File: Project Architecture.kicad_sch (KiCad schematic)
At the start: 0 parts

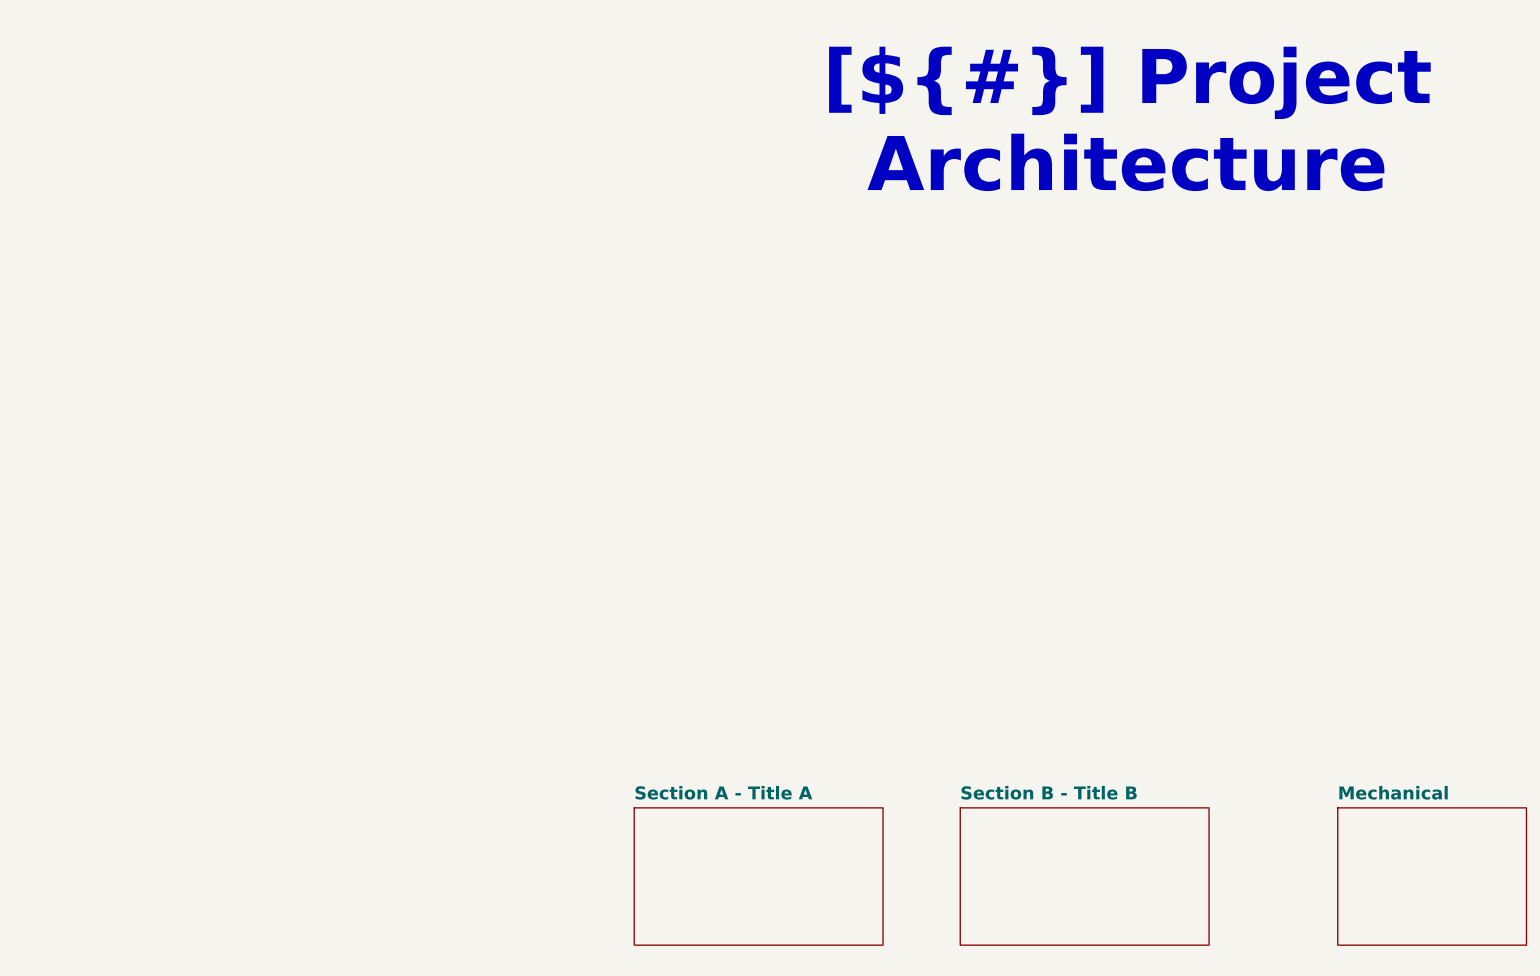
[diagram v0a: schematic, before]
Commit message: SCH[Inital Setup]: Created intital pages, added some inital symbols.
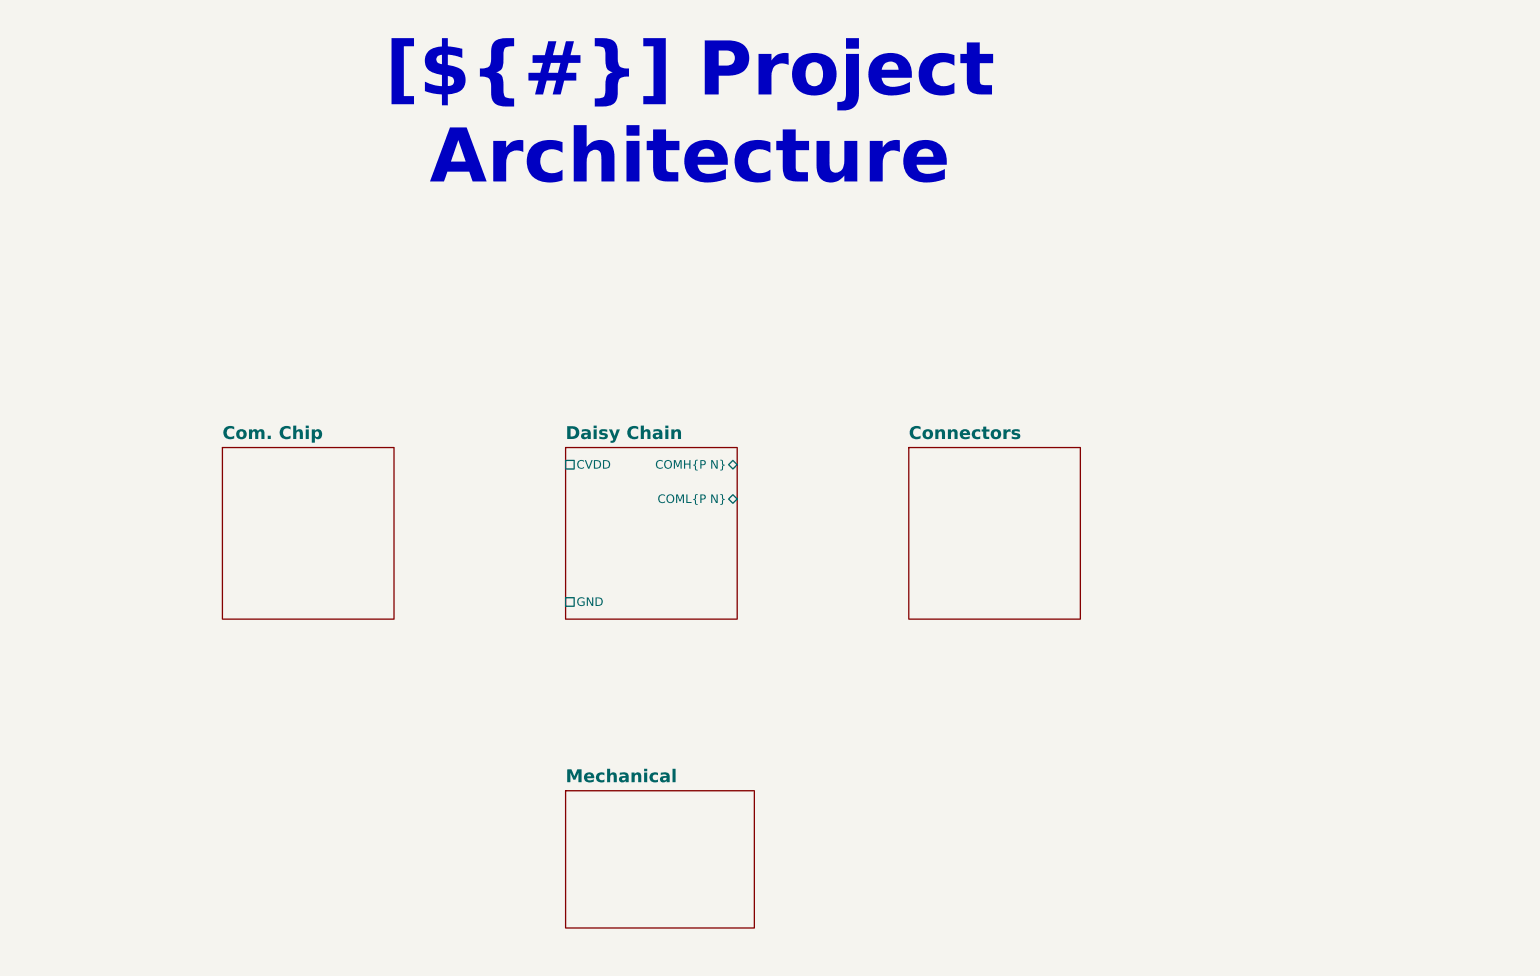
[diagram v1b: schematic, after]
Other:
- removed sheet Section A - Title A
- removed sheet Section B - Title B
- added sheet Com. Chip (com_chip.kicad_sch)
- added sheet Connectors (connectors.kicad_sch)
- added sheet Daisy Chain (daisy_chain.kicad_sch)
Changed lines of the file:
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@@
 	(generator "eeschema")
 	(generator_version "10.0")
-	(paper "A3")
+	(paper "A4")
 	(title_block
 		(title "Project Architecture")
@@
 	(text_box "[${#}] ${TITLE}"
 		(exclude_from_sim no)
-		(at 144.78 21.59 0)
+		(at 80.01 20.32 0)
 		(size 130.81 12.7)
 		(margins 5.9999 5.9999 5.9999 5.9999)
@@
 	)
 	(sheet
-		(at 241.3 129.54)
+		(at 177.8 76.2)
+		(size 25.4 25.4)
+		(exclude_from_sim no)
+		(in_bom yes)
+		(on_board yes)
+		(dnp no)
+		(fields_autoplaced yes)
+		(stroke
+			(width 0.1524)
+			(type solid)
+		)
+		(fill
+			(color 255 255 194 1)
+		)
+		(property "Sheetname" "Connectors"
+			(at 177.8 75.1709 0)
+			(show_name no)
+			(do_not_autoplace no)
+			(effects
+				(font
+					(size 1.905 1.905)
+					(thickness 0.254)
+					(bold yes)
+				)
+				(justify left bottom)
+			)
+		)
+		(property "Sheetfile" "connectors.kicad_sch"
+			(at 177.8 102.1846 0)
+			(hide yes)
+			(show_name no)
+			(do_not_autoplace no)
+			(effects
+				(font
+					(size 1.27 1.27)
+				)
+				(justify left top)
+			)
+		)
+		(instances
+			(project "bms_master"
+				(path "/f9e05184-c88b-4a88-ae9c-ab2bdb32be7c/c5103ceb-5325-4a84-a025-9638a412984e"
+					(page "4")
+				)
+			)
+		)
+	)
+	(sheet
+		(at 127 76.2)
+		(size 25.4 25.4)
+		(exclude_from_sim no)
+		(in_bom yes)
+		(on_board yes)
+		(dnp no)
+		(fields_autoplaced yes)
+		(stroke
+			(width 0)
+			(type solid)
+		)
+		(fill
+			(color 255 255 194 1)
+		)
+		(property "Sheetname" "Daisy Chain"
+			(at 127 75.1709 0)
+			(show_name no)
+			(do_not_autoplace no)
+			(effects
+				(font
+					(size 1.905 1.905)
+					(thickness 0.254)
+					(bold yes)
+				)
+				(justify left bottom)
+			)
+		)
+		(property "Sheetfile" "daisy_chain.kicad_sch"
+			(at 127 102.1846 0)
+			(hide yes)
+			(show_name no)
+			(do_not_autoplace no)
+			(effects
+				(font
+					(size 1.27 1.27)
+				)
+				(justify left top)
+			)
+		)
+		(pin "CVDD" passive
+			(at 127 78.74 180)
+			(effects
+				(font
+					(size 1.27 1.27)
+				)
+				(justify left)
+			)
+		)
+		(pin "GND" passive
+			(at 127 99.06 180)
+			(effects
+				(font
+					(size 1.27 1.27)
+				)
+				(justify left)
+			)
+		)
+		(pin "COMH{P N}" bidirectional
+			(at 152.4 78.74 0)
+			(effects
+				(font
+					(size 1.27 1.27)
+				)
+				(justify right)
+			)
+		)
+		(pin "COML{P N}" bidirectional
+			(at 152.4 83.82 0)
+			(effects
+				(font
+					(size 1.27 1.27)
+				)
+				(justify right)
+			)
+		)
+		(instances
+			(project "bms_master"
+				(path "/f9e05184-c88b-4a88-ae9c-ab2bdb32be7c/c5103ceb-5325-4a84-a025-9638a412984e"
+					(page "6")
+				)
+			)
+		)
+	)
+	(sheet
+		(at 127 127)
 		(size 27.94 20.32)
 		(exclude_from_sim no)
@@
 		)
 		(property "Sheetname" "Mechanical"
-			(at 241.3 128.5109 0)
+			(at 127 125.9709 0)
 			(show_name no)
 			(do_not_autoplace no)
@@
 		)
 		(property "Sheetfile" "mechanical.kicad_sch"
-			(at 241.3 150.4446 0)
-			(hide yes)
-			(show_name no)
-			(do_not_autoplace no)
-			(effects
-				(font
-					(size 1.27 1.27)
-				)
-				(justify left top)
-			)
-		)
-		(instances
-			(project "BOARD_TEMPLATE"
-				(path "/f9e05184-c88b-4a88-ae9c-ab2bdb32be7c/c5103ceb-5325-4a84-a025-9638a412984e"
-					(page "6")
-				)
-			)
-		)
-	)
-	(sheet
-		(at 185.42 129.54)
-		(size 36.83 20.32)
-		(exclude_from_sim no)
-		(in_bom yes)
-		(on_board yes)
-		(dnp no)
-		(fields_autoplaced yes)
-		(stroke
-			(width 0)
-			(type solid)
-		)
-		(fill
-			(color 255 255 194 1)
-		)
-		(property "Sheetname" "Section B - Title B"
-			(at 185.42 128.5109 0)
-			(show_name no)
-			(do_not_autoplace no)
-			(effects
-				(font
-					(size 1.905 1.905)
-					(bold yes)
-				)
-				(justify left bottom)
-			)
-		)
-		(property "Sheetfile" "Section B - Title B.kicad_sch"
-			(at 185.42 150.4446 0)
-			(hide yes)
-			(show_name no)
-			(do_not_autoplace no)
-			(effects
-				(font
-					(face "Arial")
-					(size 1.27 1.27)
-				)
-				(justify left top)
-			)
-		)
-		(instances
-			(project "BOARD_TEMPLATE"
+			(at 127 147.9046 0)
+			(hide yes)
+			(show_name no)
+			(do_not_autoplace no)
+			(effects
+				(font
+					(size 1.27 1.27)
+				)
+				(justify left top)
+			)
+		)
+		(instances
+			(project "bms_master"
+				(path "/f9e05184-c88b-4a88-ae9c-ab2bdb32be7c/c5103ceb-5325-4a84-a025-9638a412984e"
+					(page "8")
+				)
+			)
+		)
+	)
+	(sheet
+		(at 76.2 76.2)
+		(size 25.4 25.4)
+		(exclude_from_sim no)
+		(in_bom yes)
+		(on_board yes)
+		(dnp no)
+		(fields_autoplaced yes)
+		(stroke
+			(width 0.1524)
+			(type solid)
+		)
+		(fill
+			(color 255 255 194 1)
+		)
+		(property "Sheetname" "Com. Chip"
+			(at 76.2 75.1709 0)
+			(show_name no)
+			(do_not_autoplace no)
+			(effects
+				(font
+					(size 1.905 1.905)
+					(thickness 0.254)
+					(bold yes)
+				)
+				(justify left bottom)
+			)
+		)
+		(property "Sheetfile" "com_chip.kicad_sch"
+			(at 76.2 102.1846 0)
+			(hide yes)
+			(show_name no)
+			(do_not_autoplace no)
+			(effects
+				(font
+					(size 1.27 1.27)
+				)
+				(justify left top)
+			)
+		)
+		(instances
+			(project "bms_master"
 				(path "/f9e05184-c88b-4a88-ae9c-ab2bdb32be7c/c5103ceb-5325-4a84-a025-9638a412984e"
 					(page "5")
 				)
 			)
-		)
-	)
-	(sheet
-		(at 137.16 129.54)
-		(size 36.83 20.32)
-		(exclude_from_sim no)
-		(in_bom yes)
-		(on_board yes)
-		(dnp no)
-		(fields_autoplaced yes)
-		(stroke
-			(width 0)
-			(type solid)
-		)
-		(fill
-			(color 255 255 194 1)
-		)
-		(property "Sheetname" "Section A - Title A"
-			(at 137.16 128.5109 0)
-			(show_name no)
-			(do_not_autoplace no)
-			(effects
-				(font
-					(size 1.905 1.905)
-					(bold yes)
-				)
-				(justify left bottom)
-			)
-		)
-		(property "Sheetfile" "Section A - Title A.kicad_sch"
-			(at 137.16 150.4446 0)
-			(hide yes)
-			(show_name no)
-			(do_not_autoplace no)
-			(effects
-				(font
-					(face "Arial")
-					(size 1.27 1.27)
-				)
-				(justify left top)
-			)
-		)
-		(instances
-			(project "BOARD_TEMPLATE"
-				(path "/f9e05184-c88b-4a88-ae9c-ab2bdb32be7c/c5103ceb-5325-4a84-a025-9638a412984e"
-					(page "4")
-				)
-			)

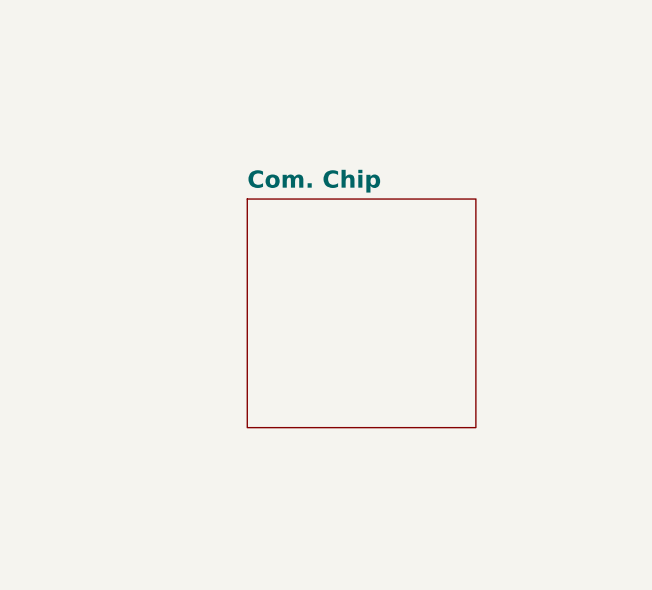
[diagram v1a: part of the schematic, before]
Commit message: SCH[Connecotr]: Added tim pinout.
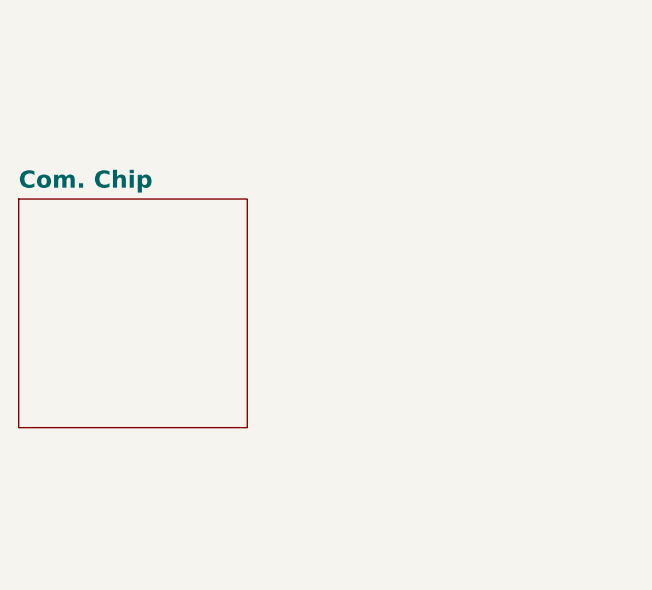
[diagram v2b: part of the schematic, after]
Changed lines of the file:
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@@
 	)
 	(sheet
-		(at 76.2 76.2)
+		(at 50.8 76.2)
 		(size 25.4 25.4)
 		(exclude_from_sim no)
@@
 		)
 		(property "Sheetname" "Com. Chip"
-			(at 76.2 75.1709 0)
+			(at 50.8 75.1709 0)
 			(show_name no)
 			(do_not_autoplace no)
@@
 		)
 		(property "Sheetfile" "com_chip.kicad_sch"
-			(at 76.2 102.1846 0)
+			(at 50.8 102.1846 0)
 			(hide yes)
 			(show_name no)

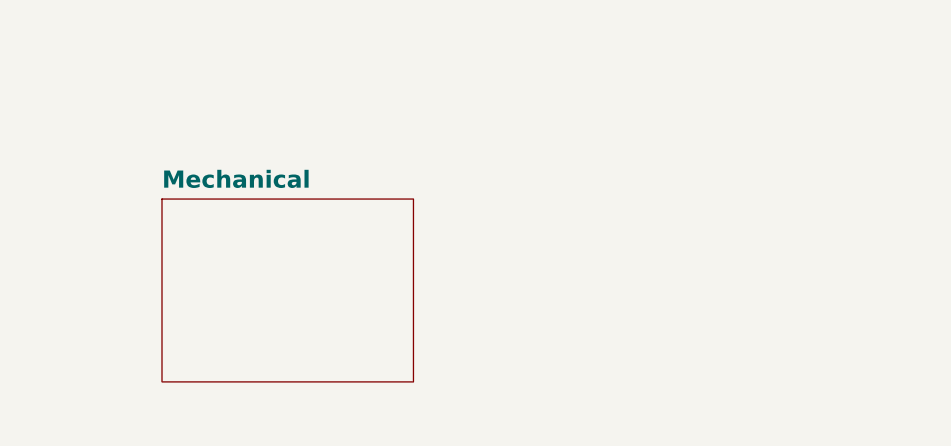
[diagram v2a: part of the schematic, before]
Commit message: SCH[Pages, Chips]: Created page setup, and placed main IC's.
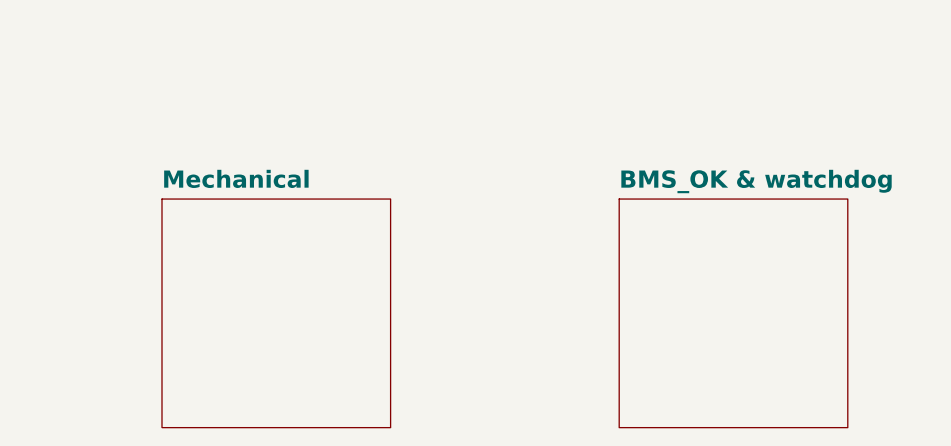
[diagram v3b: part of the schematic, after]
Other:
- added sheet BMS_OK & watchdog (bms_ok_and_watchdog.kicad_sch)
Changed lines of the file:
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@@
+	)
+	(sheet
+		(at 177.8 127)
+		(size 25.4 25.4)
+		(exclude_from_sim no)
+		(in_bom yes)
+		(on_board yes)
+		(dnp no)
+		(fields_autoplaced yes)
+		(stroke
+			(width 0)
+			(type solid)
+		)
+		(fill
+			(color 255 255 194 1)
+		)
+		(property "Sheetname" "BMS_OK & watchdog"
+			(at 177.8 125.9709 0)
+			(show_name no)
+			(do_not_autoplace no)
+			(effects
+				(font
+					(size 1.905 1.905)
+					(thickness 0.381)
+					(bold yes)
+				)
+				(justify left bottom)
+			)
+		)
+		(property "Sheetfile" "bms_ok_and_watchdog.kicad_sch"
+			(at 177.8 152.9846 0)
+			(hide yes)
+			(show_name no)
+			(do_not_autoplace no)
+			(effects
+				(font
+					(size 1.27 1.27)
+				)
+				(justify left top)
+			)
+		)
+		(instances
+			(project "bms_master"
+				(path "/f9e05184-c88b-4a88-ae9c-ab2bdb32be7c/c5103ceb-5325-4a84-a025-9638a412984e"
+					(page "7")
+				)
+			)
+		)
 	)
 	(sheet
@@
 	(sheet
 		(at 127 127)
-		(size 27.94 20.32)
+		(size 25.4 25.4)
 		(exclude_from_sim no)
 		(in_bom yes)
@@
 		)
 		(property "Sheetfile" "mechanical.kicad_sch"
-			(at 127 147.9046 0)
-			(hide yes)
-			(show_name no)
+			(at 127 152.9846 0)
+			(hide yes)
+			(show_name no)
